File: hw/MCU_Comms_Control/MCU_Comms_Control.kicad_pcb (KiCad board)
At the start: 4 copper layers, 46.7 x 68.8 mm, 55 parts, among them J1 USB_B_Mini, J2 CAN BUS, J3 TO_POWER_BOARD, J4 Mini-Debugging, J5 MULTI, SW1 BOOT, SW2 BUTTON, U1 SRV05-4, U2 SN65HVD230, U3 W25Q128JVS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

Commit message: adjustments made on silkscreen layer
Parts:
- moved G*** 6.35 mm to (90.2, 83.8)
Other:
- board text added: "PEGASUS Motor Controller v1 11/2020 PEDRO H. C. KOPPER GABRIEL GOSMANN"
- board text removed: "PEGASUS Motor Controller v1 11/2020"
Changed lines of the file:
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@@
     (34 B.Paste user hide)
     (35 F.Paste user hide)
-    (36 B.SilkS user hide)
+    (36 B.SilkS user)
     (37 F.SilkS user)
     (38 B.Mask user hide)
@@
   )
   (module Custom:pegasus_large (layer B.Cu)
-    (at 90.17 77.47 180)
+    (at 90.17 83.82 180)
     (fp_text reference G*** (at 0 0) (layer B.SilkS) hide
       (effects (font (size 1.524 1.524) (thickness 0.3)) (justify mirror))
@@
     )
   )
-  (gr_text "PEGASUS Motor Controller\nv1 11/2020" (at 89.662 58.42) (layer B.SilkS)
+  (gr_text "PEGASUS Motor Controller\nv1 11/2020\n\nPEDRO H. C. KOPPER\nGABRIEL GOSMANN" (at 90.805 62.23) (layer B.SilkS)
     (effects (font (size 2 2) (thickness 0.4)) (justify mirror))
   )

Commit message: remove old gerbers and assembly files
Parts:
- added J6: TEMP, Connector_PinHeader_2.54mm:PinHeader_2x02_P2.54mm_Vertical, F.Cu at (107.7, 73.9)
- J1: footprint Connector_USB:USB_Micro-B_Molex-105017-0001 -> Connector_USB:USB_Micro-B_Molex-105133-0001
- moved J5 6.10 mm to (110.2, 58.9)
- moved C5 3.30 mm to (102.1, 48.3)
- moved U7 3.30 mm to (105.7, 53.3)
- moved U1 2.50 mm to (103.6, 97.8)
- moved J4 2.29 mm to (110.2, 88.9)
- moved R2 2.29 mm to (109.5, 91.9)
- moved J1 2.03 mm to (109.5, 97.3)
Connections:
- net USB_DM renamed USB_D-
- net USB_DP renamed USB_D+
- J3 pad 7: Net-(J3-Pad7) -> NTC_PWR
- U4 pad 12: Net-(U4-Pad12) -> NTC_PWR
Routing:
- net Net-(J6-Pad2): track 0.00 -> 25.0 mm
- net Net-(J6-Pad1): track 0.00 -> 23.8 mm
- net NTC_PWR: track 0.00 -> 19.8 mm, vias 0 -> 2
- net MULTI0: track 27.5 -> 35.2 mm
- net MULTI1: track 29.5 -> 36.8 mm
- net Net-(C1-Pad1): track 30.0 -> 33.9 mm
- net Net-(C7-Pad1): track 8.16 -> 11.5 mm
- net USB_D-: track 21.3 -> 24.4 mm
- net USB_D+: track 19.4 -> 21.5 mm
- net HALL3: track 21.8 -> 20.5 mm
- net SWCLK: track 14.4 -> 13.4 mm
- net Net-(D1-Pad2): track 15.2 -> 14.3 mm
- net SWO: track 18.5 -> 17.6 mm
- net BUTTON: track 70.1 -> 69.2 mm
- net SWDIO: track 25.1 -> 24.4 mm
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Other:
- net class USB added: clearance 0.2032, trace_width 0.254, via_dia 0.8, via_drill 0.4
- board text added: "PEGASUS Motor Controller v1 11/2020 PEDRO KOPPER GABRIEL GOSMANN"
- board text added: "TEMP"
- board text removed: "PEGASUS Motor Controller v1 11/2020 PEDRO H. C. KOPPER GABRIEL GOSMANN"

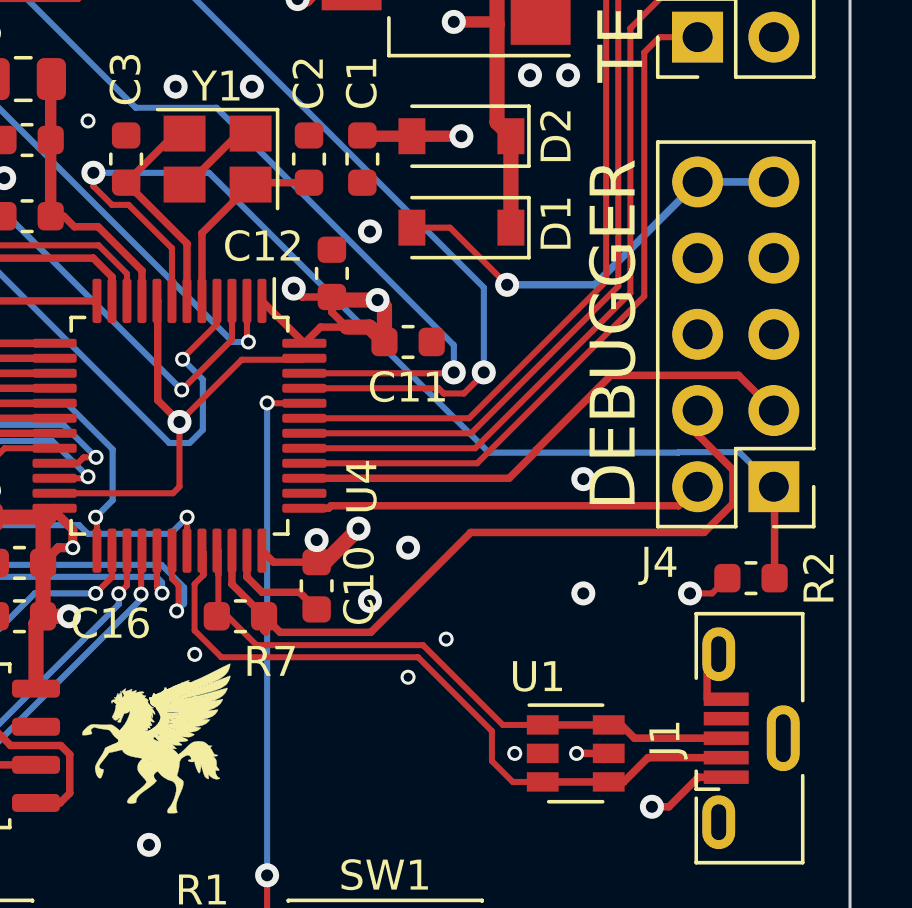
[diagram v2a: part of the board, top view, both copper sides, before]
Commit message: new mcu board revision
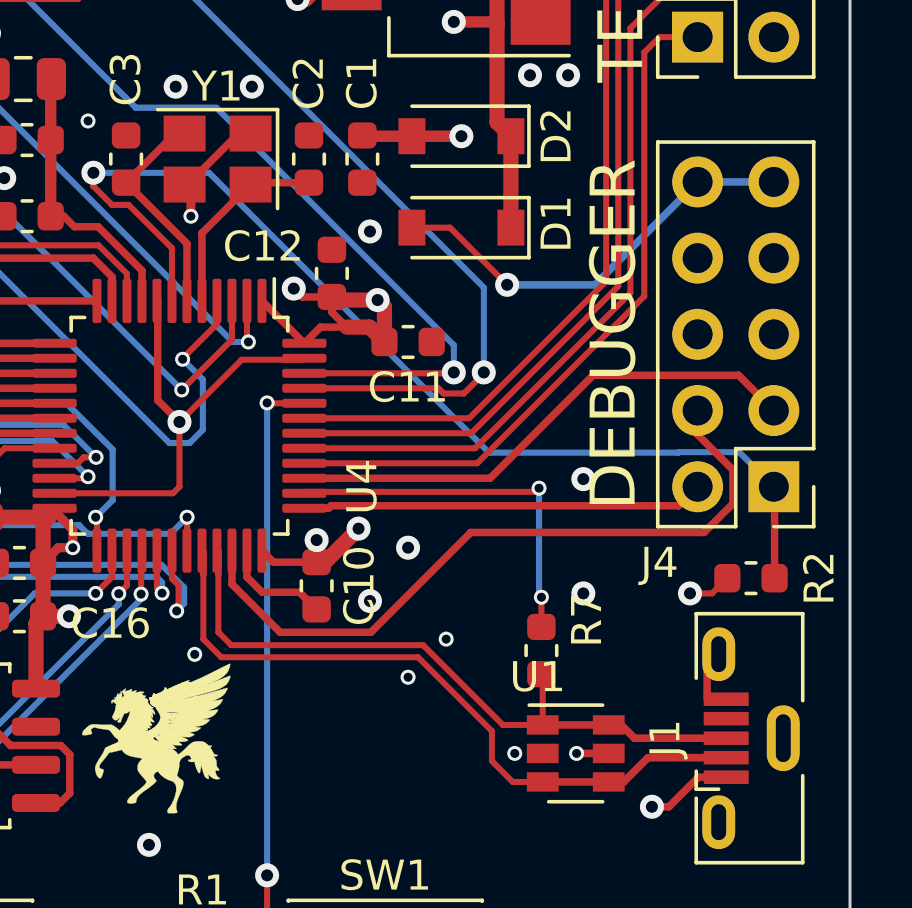
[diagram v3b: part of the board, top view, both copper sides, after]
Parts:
- moved R7 10.1 mm to (102.5, 94.4), turned to 90 degrees
- moved G*** 1.27 mm to (90.2, 85.1)
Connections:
- R7 pad 2: SWDIO -> Net-(R7-Pad2)
- U4 pad 38: Net-(U4-Pad38) -> Net-(R7-Pad2)
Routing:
- net Net-(R7-Pad2): track 0.00 -> 12.6 mm, vias 0 -> 2
- net USB_D+: track 21.5 -> 23.7 mm
- net GND: track 46.5 -> 47.6 mm, vias 46 -> 47
- net SWDIO: track 24.4 -> 23.8 mm
